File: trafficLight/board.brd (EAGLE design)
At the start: 68.6 x 53.3 mm, 7 parts

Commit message: board update
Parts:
- added R4, R5: 1k‎Ω, AUTODESK_CIRCUITS_BREADBOARD:0207/10
- added R6: 10k‎Ω, AUTODESK_CIRCUITS_BREADBOARD:0207/10
- added U2: (no value), AUTODESK_CIRCUITS_BREADBOARD:2X4P-2.54-65/35MIL
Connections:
- new net N$1: R4.1, R5.2, U2.1
- new net N$10: D4.A, U1.13
- new net N$11: D1.A, U1.11
- new net N$12: D3.A, U1.12
- new net N$4: R6.2, U2.6, U2.8
- new net N$9: D4.K, R1.2
- net N$2: now also R5.1, U1.GND.., U2.4; no longer D1.K, R1.2
- net N$3: now also R6.1, U1.3.3V; no longer D1.A, U1.13
- net N$5: now also U1.3, U2.5; no longer D3.A, U1.9
- net N$6: now also R4.2, U1.2; no longer D4.K, R3.2
- net N$7: now also D1.K, R3.2; no longer D4.A, U1.8
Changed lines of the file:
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@@
 </autorouter>
 <elements>
-<element value="" name="U1" library="AUTODESK_CIRCUITS_BREADBOARD" package="ARDUINO_UNO" x="5" y="10.08"></element><element value="" name="D1" library="AUTODESK_CIRCUITS_BREADBOARD" package="LED5MM" x="5" y="22.78"></element><element value="220‎Ω" name="R1" library="AUTODESK_CIRCUITS_BREADBOARD" package="0207/10" x="5" y="35.480000000000004"></element><element value="" name="D3" library="AUTODESK_CIRCUITS_BREADBOARD" package="LED5MM" x="5" y="48.18"></element><element value="" name="D4" library="AUTODESK_CIRCUITS_BREADBOARD" package="LED5MM" x="5" y="60.879999999999995"></element><element value="220‎Ω" name="R2" library="AUTODESK_CIRCUITS_BREADBOARD" package="0207/10" x="5" y="73.58"></element><element value="220‎Ω" name="R3" library="AUTODESK_CIRCUITS_BREADBOARD" package="0207/10" x="5" y="86.28"></element></elements>
+<element value="" name="U1" library="AUTODESK_CIRCUITS_BREADBOARD" package="ARDUINO_UNO" x="5" y="10.08"></element><element value="" name="D1" library="AUTODESK_CIRCUITS_BREADBOARD" package="LED5MM" x="5" y="22.78"></element><element value="220‎Ω" name="R1" library="AUTODESK_CIRCUITS_BREADBOARD" package="0207/10" x="5" y="35.480000000000004"></element><element value="" name="D3" library="AUTODESK_CIRCUITS_BREADBOARD" package="LED5MM" x="5" y="48.18"></element><element value="" name="D4" library="AUTODESK_CIRCUITS_BREADBOARD" package="LED5MM" x="5" y="60.879999999999995"></element><element value="220‎Ω" name="R2" library="AUTODESK_CIRCUITS_BREADBOARD" package="0207/10" x="5" y="73.58"></element><element value="220‎Ω" name="R3" library="AUTODESK_CIRCUITS_BREADBOARD" package="0207/10" x="5" y="86.28"></element><element value="" name="U2" library="AUTODESK_CIRCUITS_BREADBOARD" package="2X4P-2.54-65/35MIL" x="5" y="98.98"></element><element value="1k‎Ω" name="R4" library="AUTODESK_CIRCUITS_BREADBOARD" package="0207/10" x="5" y="111.68"></element><element value="1k‎Ω" name="R5" library="AUTODESK_CIRCUITS_BREADBOARD" package="0207/10" x="5" y="124.38000000000001"></element><element value="10k‎Ω" name="R6" library="AUTODESK_CIRCUITS_BREADBOARD" package="0207/10" x="5" y="137.08"></element></elements>
 <signals>
-<signal name="N$1"><contactref element="R1" pad="1"></contactref><contactref element="U1" pad="GND"></contactref><wire x1="-0.08000000000000007" y1="35.480000000000004" x2="31.416" y2="60.879999999999995" width="0" layer="19" extent="1-1"></wire><contactref element="R2" pad="1"></contactref><wire x1="31.416" y1="60.879999999999995" x2="-0.08000000000000007" y2="73.58" width="0" layer="19" extent="1-1"></wire><contactref element="R3" pad="1"></contactref><wire x1="-0.08000000000000007" y1="73.58" x2="-0.08000000000000007" y2="86.28" width="0" layer="19" extent="1-1"></wire></signal><signal name="N$2"><contactref element="R1" pad="2"></contactref><contactref element="D1" pad="K"></contactref><wire x1="10.08" y1="35.480000000000004" x2="6.27" y2="22.78" width="0" layer="19" extent="1-1"></wire></signal><signal name="N$3"><contactref element="D1" pad="A"></contactref><contactref element="U1" pad="13"></contactref><wire x1="3.73" y1="22.78" x2="33.956" y2="60.879999999999995" width="0" layer="19" extent="1-1"></wire></signal><signal name="N$4"><contactref element="R2" pad="2"></contactref><contactref element="D3" pad="K"></contactref><wire x1="10.08" y1="73.58" x2="6.27" y2="48.18" width="0" layer="19" extent="1-1"></wire></signal><signal name="N$5"><contactref element="D3" pad="A"></contactref><contactref element="U1" pad="9"></contactref><wire x1="3.73" y1="48.18" x2="44.116" y2="60.879999999999995" width="0" layer="19" extent="1-1"></wire></signal><signal name="N$6"><contactref element="D4" pad="K"></contactref><contactref element="R3" pad="2"></contactref><wire x1="6.27" y1="60.879999999999995" x2="10.08" y2="86.28" width="0" layer="19" extent="1-1"></wire></signal><signal name="N$7"><contactref element="D4" pad="A"></contactref><contactref element="U1" pad="8"></contactref><wire x1="3.73" y1="60.879999999999995" x2="46.656" y2="60.879999999999995" width="0" layer="19" extent="1-1"></wire></signal></signals>
+<signal name="N$1"><contactref element="R4" pad="1"></contactref><contactref element="U2" pad="1"></contactref><wire x1="-0.08000000000000007" y1="111.68" x2="3.73" y2="102.79" width="0" layer="19" extent="1-1"></wire><contactref element="R5" pad="2"></contactref><wire x1="3.73" y1="102.79" x2="10.08" y2="124.38000000000001" width="0" layer="19" extent="1-1"></wire></signal><signal name="N$2"><contactref element="R5" pad="1"></contactref><contactref element="U1" pad="GND.."></contactref><wire x1="-0.08000000000000007" y1="124.38000000000001" x2="45.64" y2="12.620000000000001" width="0" layer="19" extent="1-1"></wire><contactref element="U2" pad="4"></contactref><wire x1="45.64" y1="12.620000000000001" x2="3.73" y2="95.17" width="0" layer="19" extent="1-1"></wire></signal><signal name="N$3"><contactref element="R6" pad="1"></contactref><contactref element="U1" pad="3.3V"></contactref><wire x1="-0.08000000000000007" y1="137.08" x2="40.56" y2="12.620000000000001" width="0" layer="19" extent="1-1"></wire></signal><signal name="N$4"><contactref element="R6" pad="2"></contactref><contactref element="U2" pad="6"></contactref><wire x1="10.08" y1="137.08" x2="6.27" y2="97.71000000000001" width="0" layer="19" extent="1-1"></wire><contactref element="U2" pad="8"></contactref><wire x1="6.27" y1="97.71000000000001" x2="6.27" y2="102.79" width="0" layer="19" extent="1-1"></wire></signal><signal name="N$5"><contactref element="U2" pad="5"></contactref><contactref element="U1" pad="3"></contactref><wire x1="6.27" y1="95.17" x2="60.88" y2="60.879999999999995" width="0" layer="19" extent="1-1"></wire></signal><signal name="N$6"><contactref element="R4" pad="2"></contactref><contactref element="U1" pad="2"></contactref><wire x1="10.08" y1="111.68" x2="63.42" y2="60.879999999999995" width="0" layer="19" extent="1-1"></wire></signal><signal name="N$7"><contactref element="R3" pad="2"></contactref><contactref element="D1" pad="K"></contactref><wire x1="10.08" y1="86.28" x2="6.27" y2="22.78" width="0" layer="19" extent="1-1"></wire></signal><signal name="N$8"><contactref element="R2" pad="2"></contactref><contactref element="D3" pad="K"></contactref><wire x1="10.08" y1="73.58" x2="6.27" y2="48.18" width="0" layer="19" extent="1-1"></wire></signal><signal name="N$9"><contactref element="D4" pad="K"></contactref><contactref element="R1" pad="2"></contactref><wire x1="6.27" y1="60.879999999999995" x2="10.08" y2="35.480000000000004" width="0" layer="19" extent="1-1"></wire></signal><signal name="N$10"><contactref element="D4" pad="A"></contactref><contactref element="U1" pad="13"></contactref><wire x1="3.73" y1="60.879999999999995" x2="33.956" y2="60.879999999999995" width="0" layer="19" extent="1-1"></wire></signal><signal name="N$11"><contactref element="D1" pad="A"></contactref><contactref element="U1" pad="11"></contactref><wire x1="3.73" y1="22.78" x2="39.036" y2="60.879999999999995" width="0" layer="19" extent="1-1"></wire></signal><signal name="N$12"><contactref element="D3" pad="A"></contactref><contactref element="U1" pad="12"></contactref><wire x1="3.73" y1="48.18" x2="36.495999999999995" y2="60.879999999999995" width="0" layer="19" extent="1-1"></wire></signal><signal name="N$13"><contactref element="R3" pad="1"></contactref><contactref element="R2" pad="1"></contactref><wire x1="-0.08000000000000007" y1="86.28" x2="-0.08000000000000007" y2="73.58" width="0" layer="19" extent="1-1"></wire><contactref element="R1" pad="1"></contactref><wire x1="-0.08000000000000007" y1="73.58" x2="-0.08000000000000007" y2="35.480000000000004" width="0" layer="19" extent="1-1"></wire><contactref element="U1" pad="GND"></contactref><wire x1="-0.08000000000000007" y1="35.480000000000004" x2="31.416" y2="60.879999999999995" width="0" layer="19" extent="1-1"></wire></signal></signals>
 </board>
 </drawing>

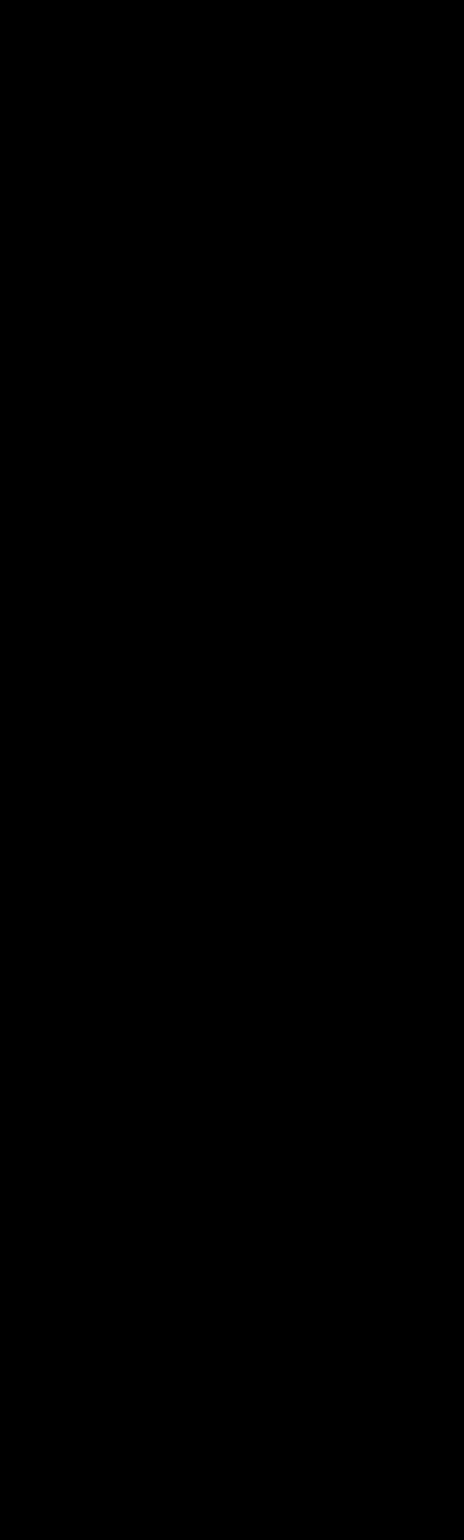
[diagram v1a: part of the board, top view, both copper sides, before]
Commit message: Adding second road ligths
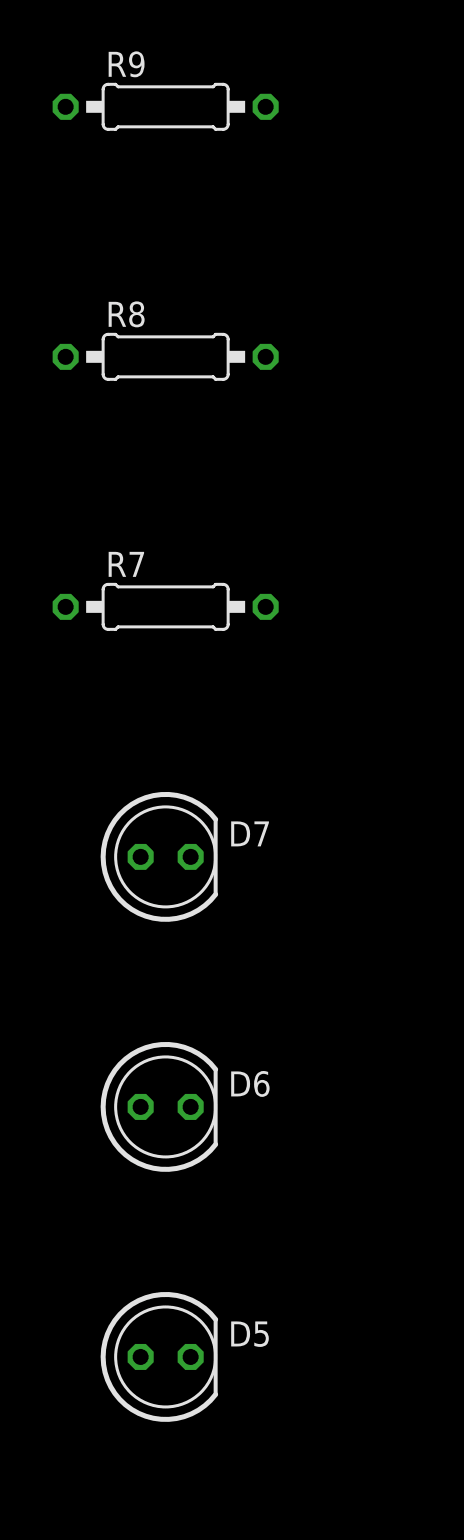
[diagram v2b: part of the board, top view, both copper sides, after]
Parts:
- added D5, D6, D7: (no value), AUTODESK_CIRCUITS_BREADBOARD:LED5MM
- added R7, R8, R9: 220‎Ω, AUTODESK_CIRCUITS_BREADBOARD:0207/10
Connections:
- new net N$14: D5.A, U1.11
- new net N$15: D6.K, R8.2
- new net N$16: D6.A, U1.12
- new net N$17: D7.K, R9.2
- new net N$18: D7.A, U1.13
- new net N$19: R1.1, R2.1, R3.1, R7.1, R8.1, R9.1, U1.GND
- net N$10: now also U1.10; no longer U1.13
- net N$11: now also U1.8; no longer U1.11
- net N$12: now also U1.9; no longer U1.12
- net N$13: now also D5.K, R7.2; no longer R1.1, R2.1, R3.1, U1.GND
